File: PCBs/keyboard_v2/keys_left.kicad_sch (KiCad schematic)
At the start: 55 parts, among them SW1201 SW_DIP_x01, SW1202 SW_DIP_x01, SW1203 SW_DIP_x01, SW1204 SW_DIP_x01, SW1205 SW_DIP_x01, SW1206 SW_DIP_x01, SW1207 SW_DIP_x01, SW1208 SW_DIP_x01, SW1209 SW_DIP_x01, SW1210 SW_DIP_x01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

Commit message: Display schematic done
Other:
- note added: "encoder should use 3.3V"
- note added: "level shifter"
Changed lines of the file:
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@@
 	(wire
 		(pts
-			(xy 22.86 35.56) (xy 27.94 35.56)
+			(xy 17.78 35.56) (xy 27.94 35.56)
 		)
 		(stroke
@@
 		)
 	)
+	(text "level shifter"
+		(exclude_from_sim no)
+		(at 43.18 170.18 0)
+		(effects
+			(font
+				(size 1.27 1.27)
+			)
+		)
+	)
+	(text "encoder should use 3.3V"
+		(exclude_from_sim no)
+		(at 190.5 170.18 0)
+		(effects
+			(font
+				(size 1.27 1.27)
+			)
+		)
+	)
 	(label "LED25"
 		(at 187.96 66.04 0)
@@
 		)
 	)
+	(label "LED1"
+		(at 50.8 170.18 0)
+		(fields_autoplaced yes)
+		(effects
+			(font
+				(size 1.27 1.27)
+			)
+			(justify left bottom)
+		)
+	)
 	(label "LED24"
 		(at 160.02 66.04 0)
@@
 		)
 	)
+	(label "LED1"
+		(at 17.78 35.56 0)
+		(fields_autoplaced yes)
+		(effects
+			(font
+				(size 1.27 1.27)
+			)
+			(justify left bottom)
+		)
+	)
 	(label "LED10"
 		(at 281.94 35.56 180)
@@
 		)
 	)
-	(hierarchical_label "LED1"
-		(shape input)
-		(at 22.86 35.56 180)
-		(fields_autoplaced yes)
-		(effects
-			(font
-				(size 1.27 1.27)
-			)
-			(justify right)
-		)
-	)
 	(hierarchical_label "KEY_D6"
 		(shape output)
@@
 		)
 	)
+	(hierarchical_label "NEOPIXEL"
+		(shape input)
+		(at 35.56 170.18 180)
+		(fields_autoplaced yes)
+		(effects
+			(font
+				(size 1.27 1.27)
+			)
+			(justify right)
+		)
+	)
 	(hierarchical_label "KEY_E2"
 		(shape output)
@@
 					(unit 1)
 				)
+			)
+		)
+	)
+	(symbol
+		(lib_id "power:VBUS")
+		(at 43.18 165.1 0)
+		(unit 1)
+		(exclude_from_sim no)
+		(in_bom yes)
+		(on_board yes)
+		(dnp no)
+		(fields_autoplaced yes)
+		(property "Reference" "#PWR01230"
+			(at 43.18 168.91 0)
+			(effects
+				(font
+					(size 1.27 1.27)
+				)
+				(hide yes)
+			)
+		)
+		(property "Value" "VBUS"
+			(at 43.18 160.02 0)
+			(effects
+				(font
+					(size 1.27 1.27)
+				)
+			)
+		)
+		(property "Footprint" ""
+			(at 43.18 165.1 0)
+			(effects
+				(font
+					(size 1.27 1.27)
+				)
+				(hide yes)
+			)
+		)
+		(property "Datasheet" ""
+			(at 43.18 165.1 0)
+			(effects
+				(font
+					(size 1.27 1.27)
+				)
+				(hide yes)
+			)
+		)
+		(property "Description" "Power symbol creates a global label with name \"VBUS\""
+			(at 43.18 165.1 0)
+			(effects
+				(font
+					(size 1.27 1.27)
+				)
+				(hide yes)
+			)
+		)
+		(pin "1"
+		)
+		(instances
+			(project "keyboard_v2"
+				(path "/e2360b7f-be71-48d9-b398-9f8cd45479d6/8d5749a2-4d36-4f17-8c57-9c8b87d773d6/434714c7-475a-4e7a-95b8-de0bbee6f731"
+					(reference "#PWR01230")
+					(unit 1)
+				)

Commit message: V2 Schematic mostly done
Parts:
- added Q1201: DMN21D2UFB-7B, keyboard_footprints:DMN21D2UFB7B, symbol DMN21D2UFB-7B:DMN21D2UFB-7B
- added R1201: 4k7, Resistor_SMD:R_0402_1005Metric, symbol Device:R_Small
- added R1204, R1208: 100k, Resistor_SMD:R_0402_1005Metric, symbol Device:R_Small
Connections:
- net ENC_A: now also R1204.2
- net ENC_B: now also R1208.2
- net LED1: now also Q1201.3 (D), R1201.2
- net NEOPIXEL: now also Q1201.2 (S)
- net VBUS: now also R1201.1
- new net +1V8: Q1201.1 (G)
- new net +VSYS: R1204.1, R1208.1
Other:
- note removed: "encoder should use 3.3V"
- note removed: "level shifter"
- moved on the sheet: SW1227

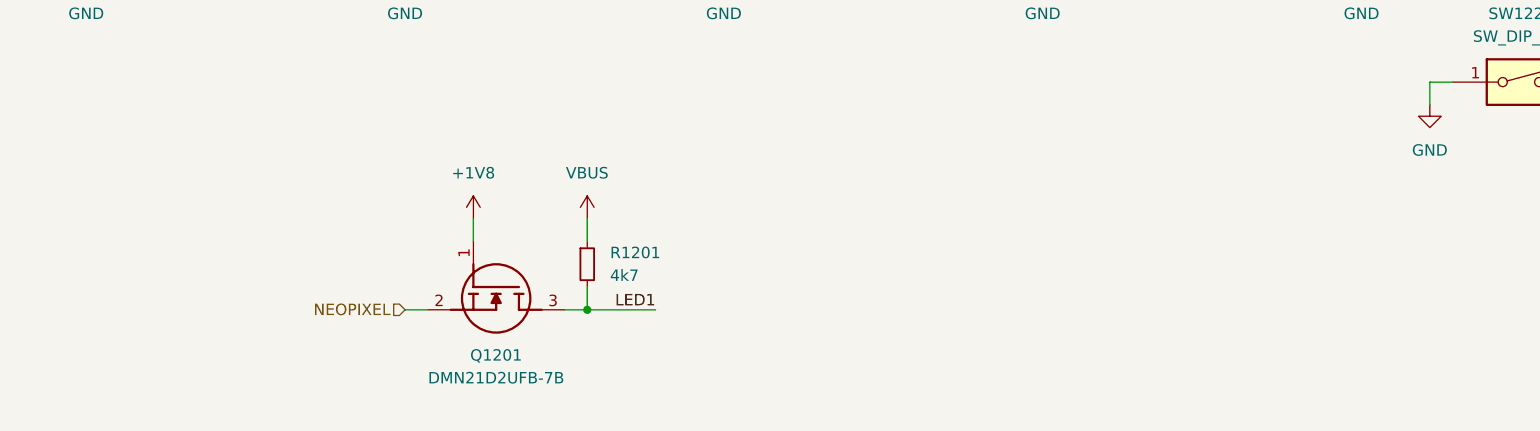
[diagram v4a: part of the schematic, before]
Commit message: Schematic mostly done, moving onto PCB
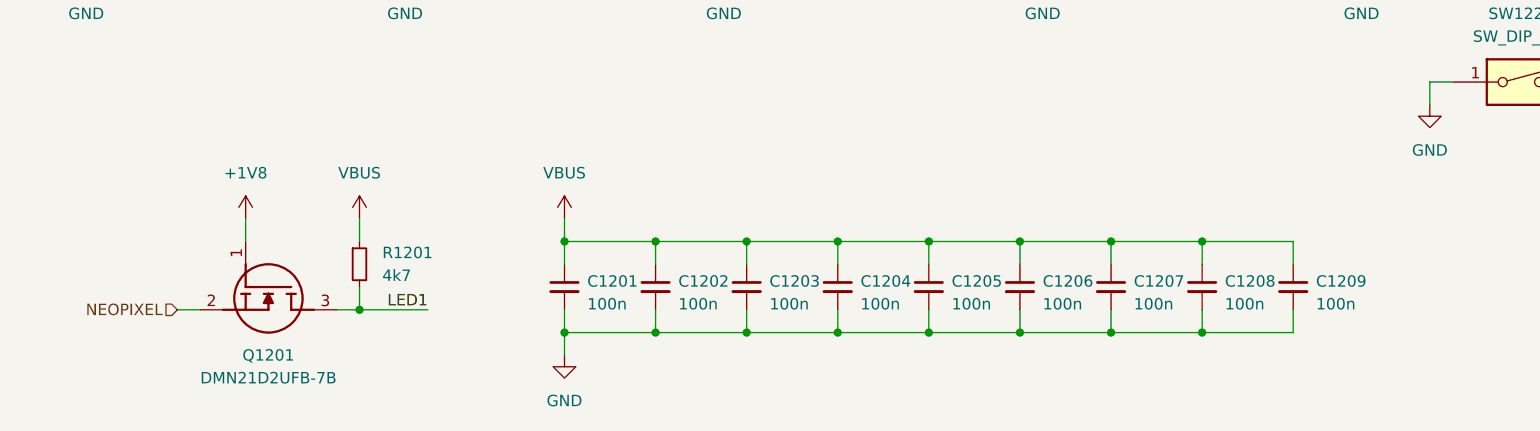
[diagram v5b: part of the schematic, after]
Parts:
- added C1201, C1202, C1203, C1204, C1205, C1206, C1207, C1208, C1209: 100n, Capacitor_SMD:C_0402_1005Metric, symbol Device:C_Small
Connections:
- net GND: now also C1201.2, C1202.2, C1203.2, C1204.2, C1205.2, C1206.2, C1207.2, C1208.2, C1209.2
- net VBUS: now also C1201.1, C1202.1, C1203.1, C1204.1, C1205.1, C1206.1, C1207.1, C1208.1, C1209.1
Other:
- moved on the sheet: Q1201, R1201
